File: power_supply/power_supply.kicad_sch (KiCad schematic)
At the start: 53 parts, among them J2 Alimentação AC, J3 SAÍDA, Q1 TIP122, T1 35VAC - 3A, U1 CA3140, U2 ICL7107CPL, U3 ICL7660, U4 LM7824_TO220, U5 LM7805_TO220

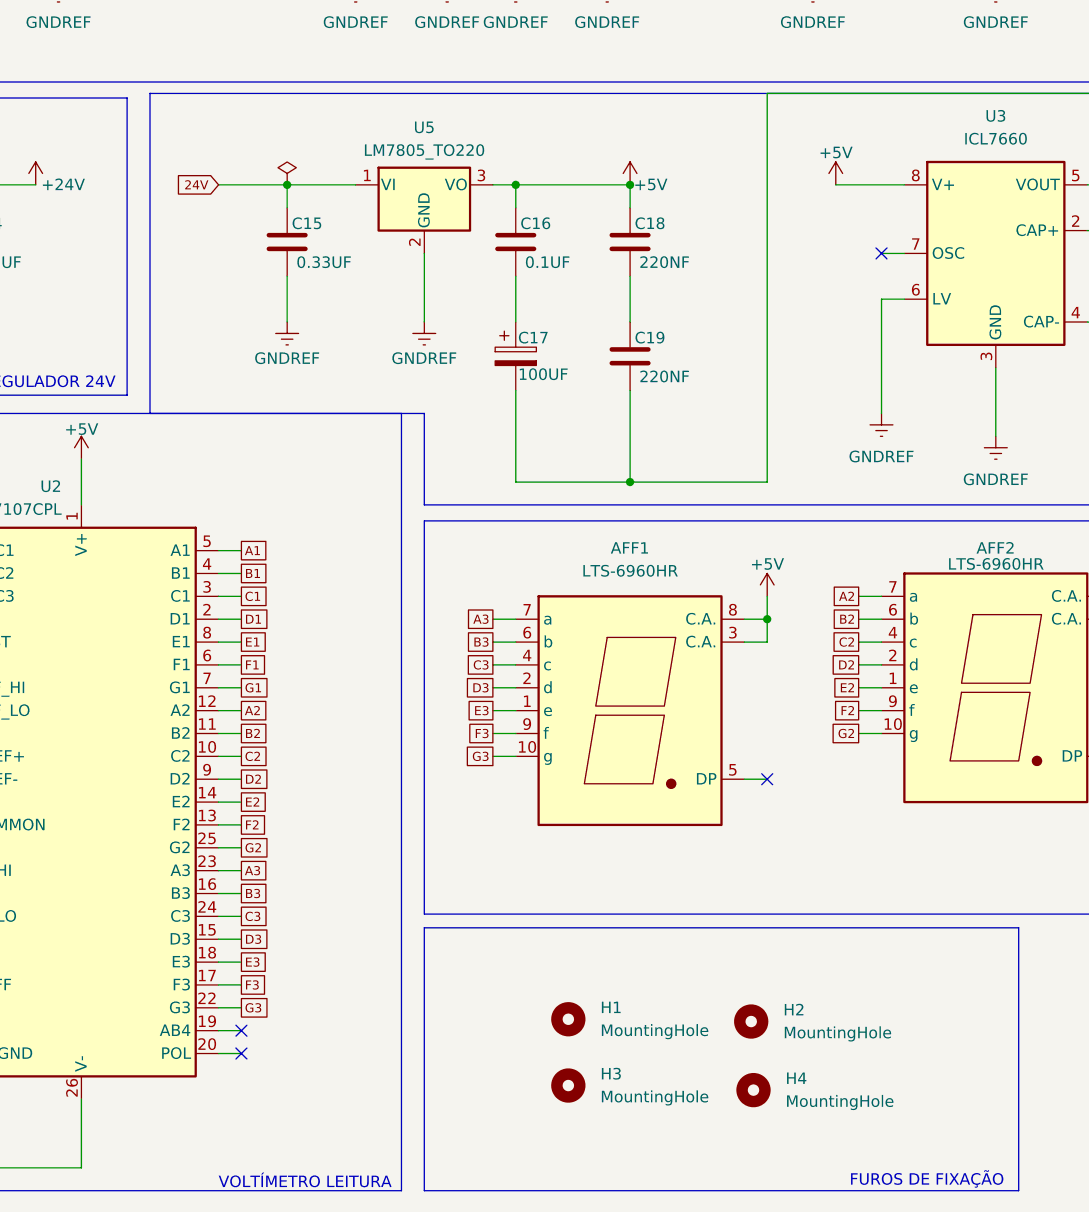
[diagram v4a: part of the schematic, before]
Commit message: Finalização do Layout, aguardando dúvida das Vias para trilhas de 3mm.
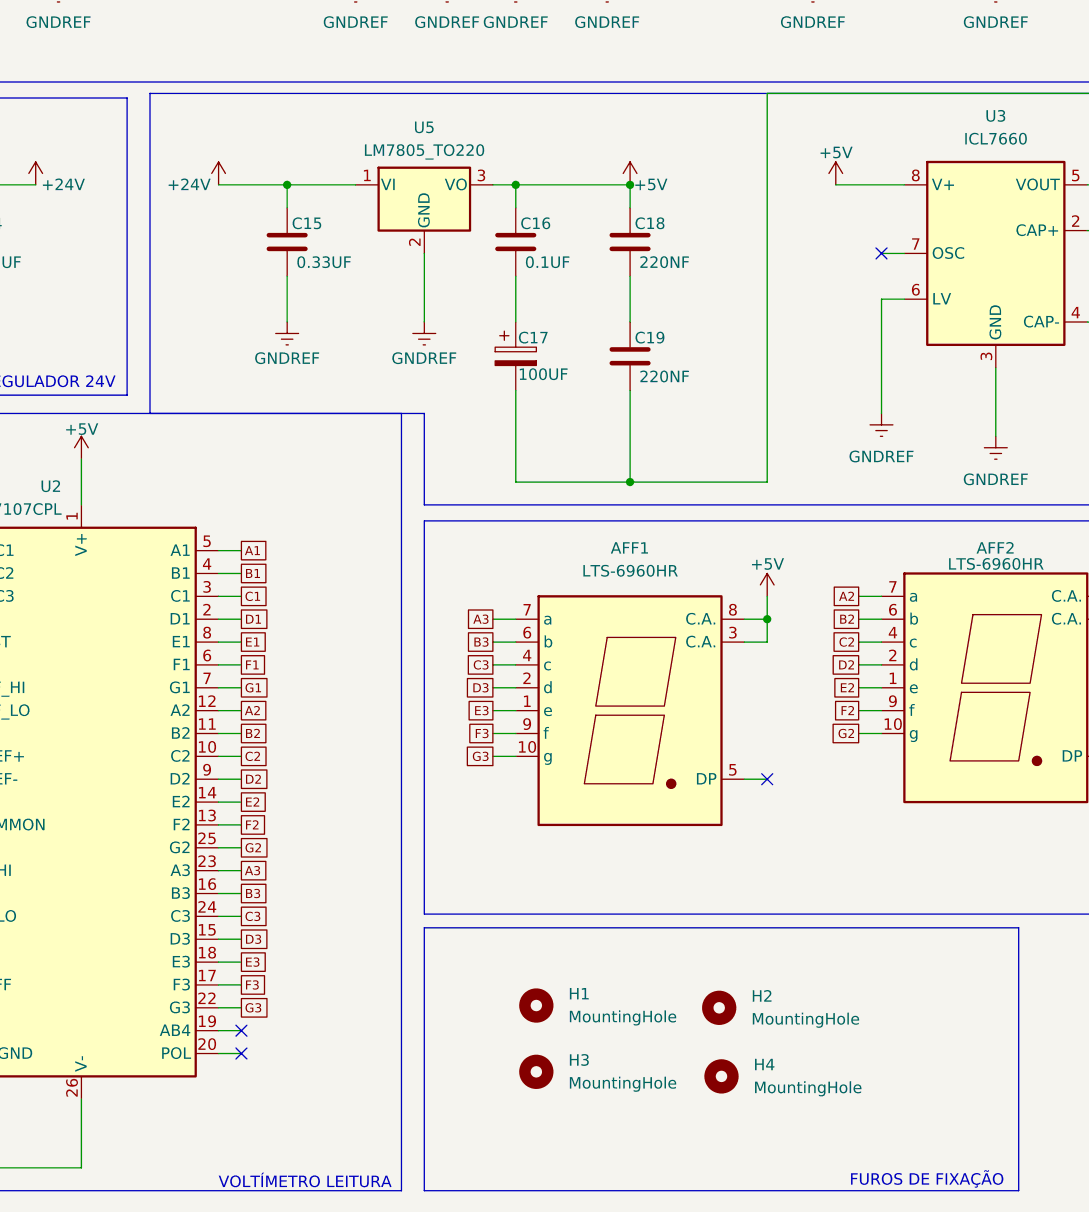
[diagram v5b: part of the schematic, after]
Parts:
- AFF1: footprint Display_7Segment:7SegmentLED_LTS6760_LTS6780 -> TestPoint:TestPoint_Pad_D2.0mm
- J3: footprint Connector:Banana_Jack_2Pin -> Connector_Molex:Molex_KK-396_5273-02A_1x02_P3.96mm_Vertical
- U2: footprint Package_QFP:MQFP-44_10x10mm_P0.8mm -> Package_DIP:DIP-40_W15.24mm
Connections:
- net 24V is gone; now on net +24V: C15.1, U5.1 (VI)
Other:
- moved on the sheet: H1, H2, H3, H4
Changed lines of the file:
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@@
-    )
-  )
-  (global_label "24V" (shape input) (at 86.36 83.82 180) (fields_autoplaced)
-    (effects (font (size 1 1)) (justify right))
-    (property "Intersheetrefs" "${INTERSHEET_REFS}" (at 81.2478 83.82 0)
-      (effects (font (size 1.27 1.27)) (justify right) hide)
     )
   )
@@
     )
   )
+  (symbol (lib_id "power:+24V") (at 86.36 83.82 0) (unit 1)
+    (in_bom yes) (on_board yes) (dnp no)
+    (property "Reference" "#PWR027" (at 86.36 87.63 0)
+      (effects (font (size 1.27 1.27)) hide)
+    )
+    (property "Value" "+24V" (at 83.058 83.82 0)
+      (effects (font (size 1.27 1.27)))
+    )
+    (property "Footprint" "" (at 86.36 83.82 0)
+      (effects (font (size 1.27 1.27)) hide)
+    )
+    (property "Datasheet" "" (at 86.36 83.82 0)
+      (effects (font (size 1.27 1.27)) hide)
+    )
+    (pin "1")
+    (instances
+      (project "power_supply"
+        (path "/22e05a20-d029-41db-9dfe-dd14f5d3b1be"
+          (reference "#PWR027") (unit 1)
+        )
+      )
+    )
+  )
   (symbol (lib_id "power:+5V") (at 33.02 132.08 0) (unit 1)
     (in_bom yes) (on_board yes) (dnp no)
@@
       (effects (font (size 1.27 1.27)))
     )
-    (property "Footprint" "Display_7Segment:7SegmentLED_LTS6760_LTS6780" (at 132.08 157.48 0)
+    (property "Footprint" "TestPoint:TestPoint_Pad_D2.0mm" (at 132.08 157.48 0)
       (effects (font (size 1.27 1.27)) hide)
     )
@@
     )
   )
-  (symbol (lib_id "power:PWR_FLAG") (at 93.98 83.82 0) (unit 1)
-    (in_bom yes) (on_board yes) (dnp no) (fields_autoplaced)
-    (property "Reference" "#FLG02" (at 93.98 81.915 0)
-      (effects (font (size 1.27 1.27)) hide)
-    )
-    (property "Value" "PWR_FLAG" (at 93.98 78.994 0)
-      (effects (font (size 1.27 1.27)) hide)
-    )
-    (property "Footprint" "" (at 93.98 83.82 0)
-      (effects (font (size 1.27 1.27)) hide)
-    )
-    (property "Datasheet" "~" (at 93.98 83.82 0)
-      (effects (font (size 1.27 1.27)) hide)
-    )
-    (pin "1")
-    (instances
-      (project "power_supply"
-        (path "/22e05a20-d029-41db-9dfe-dd14f5d3b1be"
-          (reference "#FLG02") (unit 1)
-        )
-      )
-    )
-  )
   (symbol (lib_id "Connector_Generic:Conn_01x02") (at 261.62 96.52 180) (unit 1)
     (in_bom yes) (on_board yes) (dnp no)
@@
     )
   )
-  (symbol (lib_id "Mechanical:MountingHole") (at 125.222 176.53 0) (unit 1)
-    (in_bom yes) (on_board yes) (dnp no) (fields_autoplaced)
-    (property "Reference" "H1" (at 128.778 175.26 0)
-      (effects (font (size 1.27 1.27)) (justify left))
-    )
-    (property "Value" "MountingHole" (at 128.778 177.8 0)
-      (effects (font (size 1.27 1.27)) (justify left))
-    )
-    (property "Footprint" "MountingHole:MountingHole_3.2mm_M3" (at 125.222 176.53 0)
-      (effects (font (size 1.27 1.27)) hide)
-    )
-    (property "Datasheet" "~" (at 125.222 176.53 0)
+  (symbol (lib_id "Mechanical:MountingHole") (at 121.666 175.006 0) (unit 1)
+    (in_bom yes) (on_board yes) (dnp no) (fields_autoplaced)
+    (property "Reference" "H1" (at 125.222 173.736 0)
+      (effects (font (size 1.27 1.27)) (justify left))
+    )
+    (property "Value" "MountingHole" (at 125.222 176.276 0)
+      (effects (font (size 1.27 1.27)) (justify left))
+    )
+    (property "Footprint" "MountingHole:MountingHole_3.2mm_M3" (at 121.666 175.006 0)
+      (effects (font (size 1.27 1.27)) hide)
+    )
+    (property "Datasheet" "~" (at 121.666 175.006 0)
       (effects (font (size 1.27 1.27)) hide)
     )
@@
     )
   )
-  (symbol (lib_id "Mechanical:MountingHole") (at 125.222 183.896 0) (unit 1)
-    (in_bom yes) (on_board yes) (dnp no) (fields_autoplaced)
-    (property "Reference" "H3" (at 128.778 182.626 0)
-      (effects (font (size 1.27 1.27)) (justify left))
-    )
-    (property "Value" "MountingHole" (at 128.778 185.166 0)
-      (effects (font (size 1.27 1.27)) (justify left))
-    )
-    (property "Footprint" "MountingHole:MountingHole_3.2mm_M3" (at 125.222 183.896 0)
-      (effects (font (size 1.27 1.27)) hide)
-    )
-    (property "Datasheet" "~" (at 125.222 183.896 0)
+  (symbol (lib_id "Mechanical:MountingHole") (at 121.666 182.372 0) (unit 1)
+    (in_bom yes) (on_board yes) (dnp no) (fields_autoplaced)
+    (property "Reference" "H3" (at 125.222 181.102 0)
+      (effects (font (size 1.27 1.27)) (justify left))
+    )
+    (property "Value" "MountingHole" (at 125.222 183.642 0)
+      (effects (font (size 1.27 1.27)) (justify left))
+    )
+    (property "Footprint" "MountingHole:MountingHole_3.2mm_M3" (at 121.666 182.372 0)
+      (effects (font (size 1.27 1.27)) hide)
+    )
+    (property "Datasheet" "~" (at 121.666 182.372 0)
       (effects (font (size 1.27 1.27)) hide)
     )
@@
     )
   )
-  (symbol (lib_id "Mechanical:MountingHole") (at 145.542 176.784 0) (unit 1)
-    (in_bom yes) (on_board yes) (dnp no) (fields_autoplaced)
-    (property "Reference" "H2" (at 149.098 175.514 0)
-      (effects (font (size 1.27 1.27)) (justify left))
-    )
-    (property "Value" "MountingHole" (at 149.098 178.054 0)
-      (effects (font (size 1.27 1.27)) (justify left))
-    )
-    (property "Footprint" "MountingHole:MountingHole_3.2mm_M3" (at 145.542 176.784 0)
-      (effects (font (size 1.27 1.27)) hide)
-    )
-    (property "Datasheet" "~" (at 145.542 176.784 0)
+  (symbol (lib_id "Mechanical:MountingHole") (at 141.986 175.26 0) (unit 1)
+    (in_bom yes) (on_board yes) (dnp no) (fields_autoplaced)
+    (property "Reference" "H2" (at 145.542 173.99 0)
+      (effects (font (size 1.27 1.27)) (justify left))
+    )
+    (property "Value" "MountingHole" (at 145.542 176.53 0)
+      (effects (font (size 1.27 1.27)) (justify left))
+    )
+    (property "Footprint" "MountingHole:MountingHole_3.2mm_M3" (at 141.986 175.26 0)
+      (effects (font (size 1.27 1.27)) hide)
+    )
+    (property "Datasheet" "~" (at 141.986 175.26 0)
       (effects (font (size 1.27 1.27)) hide)
     )
@@
       (effects (font (size 1.27 1.27)))
     )
-    (property "Footprint" "Connector:Banana_Jack_2Pin" (at 226.06 96.52 0)
+    (property "Footprint" "Connector_Molex:Molex_KK-396_5273-02A_1x02_P3.96mm_Vertical" (at 226.06 96.52 0)
       (effects (font (size 1.27 1.27)) hide)
     )
@@
     )
   )
-  (symbol (lib_id "Mechanical:MountingHole") (at 145.796 184.404 0) (unit 1)
-    (in_bom yes) (on_board yes) (dnp no) (fields_autoplaced)
-    (property "Reference" "H4" (at 149.352 183.134 0)
-      (effects (font (size 1.27 1.27)) (justify left))
-    )
-    (property "Value" "MountingHole" (at 149.352 185.674 0)
-      (effects (font (size 1.27 1.27)) (justify left))
-    )
-    (property "Footprint" "MountingHole:MountingHole_3.2mm_M3" (at 145.796 184.404 0)
-      (effects (font (size 1.27 1.27)) hide)
-    )
-    (property "Datasheet" "~" (at 145.796 184.404 0)
+  (symbol (lib_id "Mechanical:MountingHole") (at 142.24 182.88 0) (unit 1)
+    (in_bom yes) (on_board yes) (dnp no) (fields_autoplaced)
+    (property "Reference" "H4" (at 145.796 181.61 0)
+      (effects (font (size 1.27 1.27)) (justify left))
+    )
+    (property "Value" "MountingHole" (at 145.796 184.15 0)
+      (effects (font (size 1.27 1.27)) (justify left))
+    )
+    (property "Footprint" "MountingHole:MountingHole_3.2mm_M3" (at 142.24 182.88 0)
+      (effects (font (size 1.27 1.27)) hide)
+    )
+    (property "Datasheet" "~" (at 142.24 182.88 0)
       (effects (font (size 1.27 1.27)) hide)
     )
@@
       (effects (font (size 1.27 1.27)) (justify left))
     )
-    (property "Footprint" "Package_QFP:MQFP-44_10x10mm_P0.8mm" (at 71.12 184.15 0)
-      (effects (font (size 1.27 1.27)) hide)
-    )
+    (property "Footprint" "Package_DIP:DIP-40_W15.24mm" (at 71.12 184.15 0)
+      (effects (font (size 1.27 1.27)) hide)
+    )
